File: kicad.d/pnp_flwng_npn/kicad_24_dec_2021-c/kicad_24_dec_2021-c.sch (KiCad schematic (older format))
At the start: 30 parts, among them Q1 2N3906, SW1 SW_SPDT, U1 ULN2803A

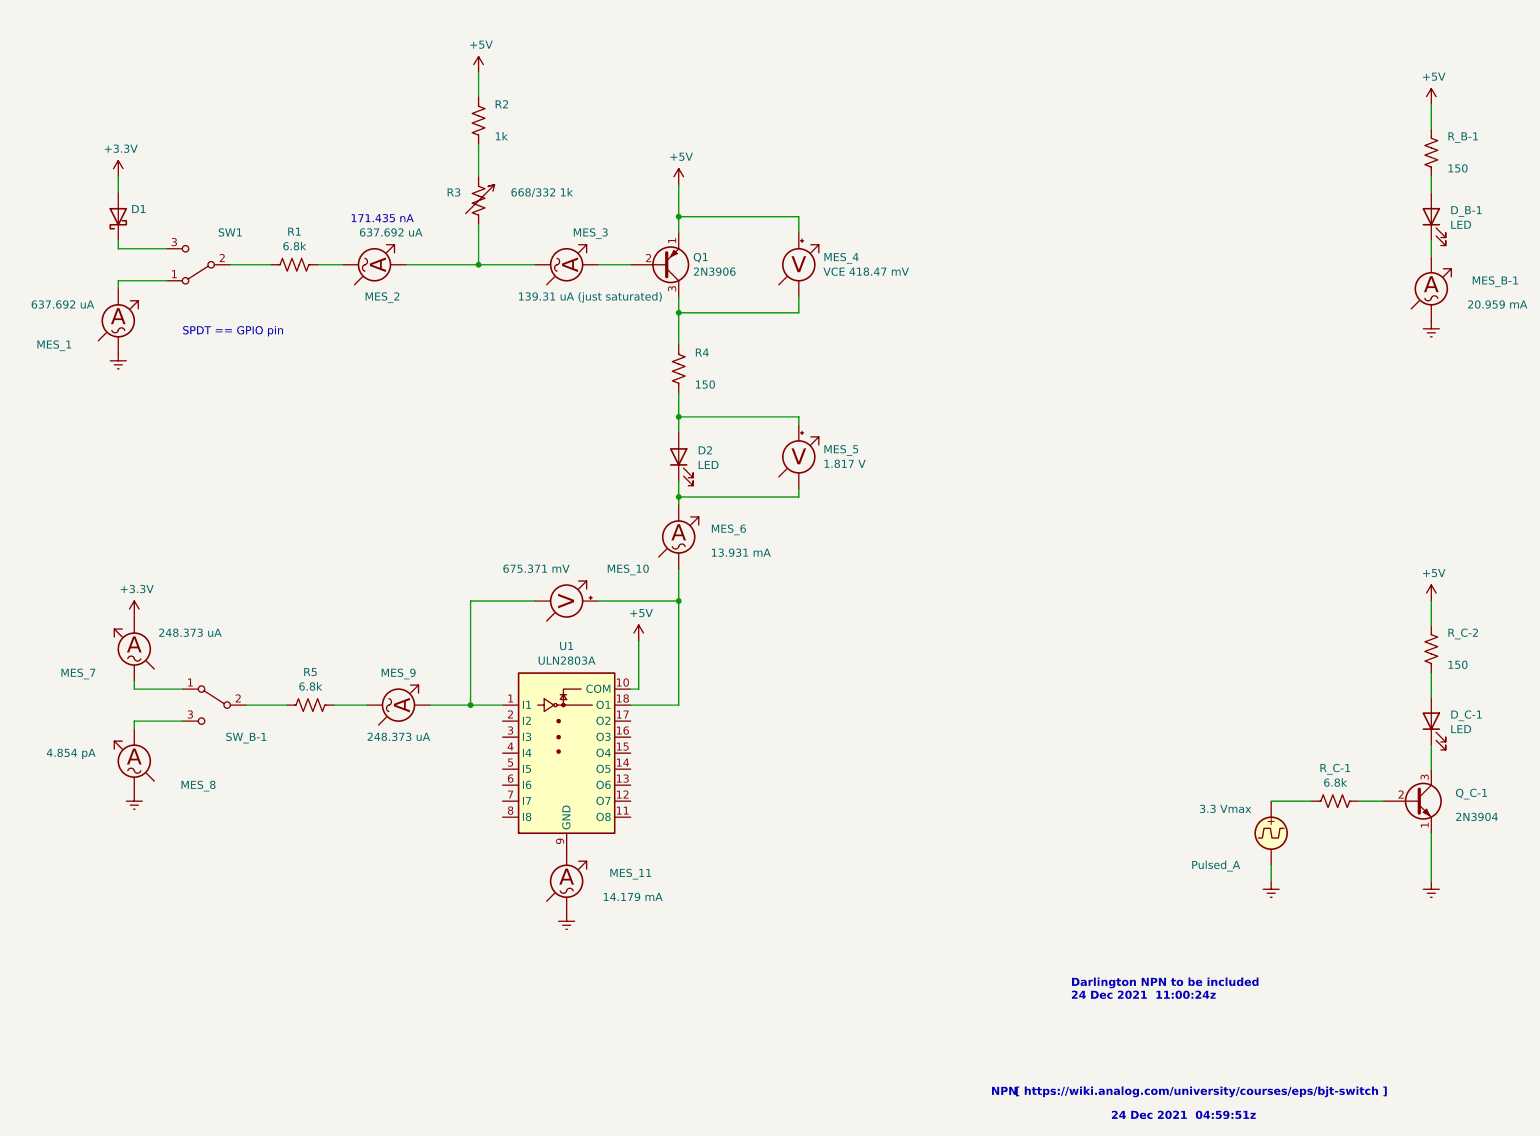
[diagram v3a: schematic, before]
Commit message: AC ammeter to DC
	modified:   kicad_24_dec_2021-c-cache.lib
	modified:   kicad_24_dec_2021-c.png
	modified:   kicad_24_dec_2021-c.sch
	modified:   kicad_24_dec_2021-c.svg

On branch dvlp-aa
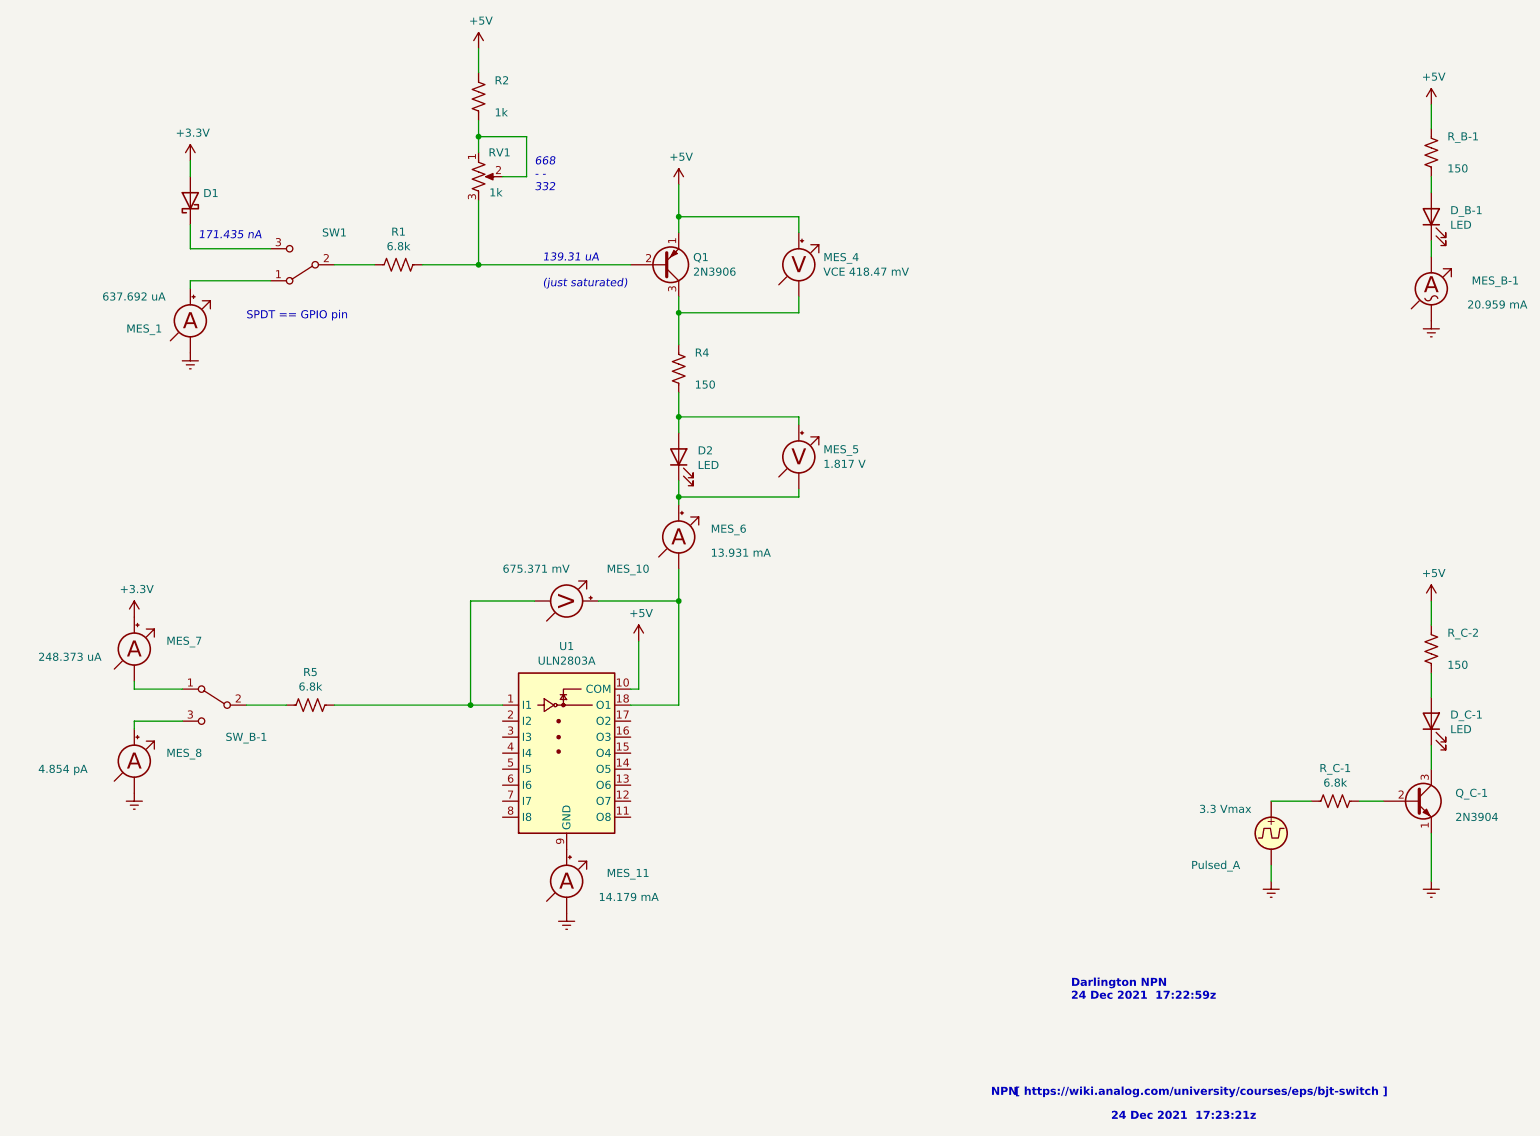
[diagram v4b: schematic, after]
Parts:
- removed MES_1, MES_2: 637.692 uA, symbol Device:Amperemeter_AC
- removed MES_11: 14.179 mA, symbol Device:Amperemeter_AC
- removed MES_3: 139.31 uA (just saturated), symbol Device:Amperemeter_AC
- removed MES_6: 13.931 mA, symbol Device:Amperemeter_AC
- removed MES_7, MES_9: 248.373 uA, symbol Device:Amperemeter_AC
- removed MES_8: 4.854 pA, symbol Device:Amperemeter_AC
- removed R3: 668/332 1k, symbol Device:R_Variable_US
- added MES_1: 637.692 uA, symbol Device:Amperemeter_DC
- added MES_11: 14.179 mA, symbol Device:Amperemeter_DC
- added MES_6: 13.931 mA, symbol Device:Amperemeter_DC
- added MES_7: 248.373 uA, symbol Device:Amperemeter_DC
- added MES_8: 4.854 pA, symbol Device:Amperemeter_DC
- added RV1: 1k, symbol Device:R_POT_US
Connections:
- net +3V3: now also MES_7.2 (+)
- net GNDREF: now also MES_1.1 (-), MES_11.1 (-), MES_8.1 (-)
- net at MES_10.1 (-), U1.1 (I1): now also R5.2
- net at MES_10.2 (+), U1.18 (O1): now also MES_6.1 (-)
- net at U1.9 (GND): now also MES_11.2 (+)
- net at D2.1 (K), MES_5.1 (-): now also MES_6.2 (+)
- net at SW_B-1.1 (A): now also MES_7.1 (-)
- net at SW_B-1.3 (C): now also MES_8.2 (+)
- net at Q1.2 (B): now also R1.2, RV1.3
- net at R2.2: now also RV1.1, RV1.2
- net at SW1.1 (A): now also MES_1.2 (+)
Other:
- note added: "139.31 uA\n\n(just saturated)"
- note added: "24 Dec 2021 17:23:21z"
- note added: "668\n- -\n332"
- note added: "Darlington NPN \n24 Dec 2021 17:22:59z"
- note removed: "24 Dec 2021 04:59:51z"
- note removed: "Darlington NPN to be included\n24 Dec 2021 11:00:24z"
- moved on the sheet: D1, R1, R2, SW1
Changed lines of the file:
@@
 $EndDescr
-$Comp
-L Device:Amperemeter_AC MES_6
-U 1 1 61D27D60
-P 5500 4000
-F 0 "MES_6" H 5700 4050 50  0000 L CNN
-F 1 "13.931 mA" H 5700 3900 50  0000 L CNN
-F 2 "" V 5500 4100 50  0001 C CNN
-F 3 "~" V 5500 4100 50  0001 C CNN
-	1    5500 4000
-	1    0    0    -1
-$EndComp
 $Comp
 L Device:LED D2
@@
  [ https://wiki.analog.com/university/courses/eps/bjt-switch ]
 Text Notes 8200 7650 0    50   ~ 10
-24 Dec 2021  04:59:51z
+24 Dec 2021  17:23:21z
 $Comp
 L Switch:SW_SPDT SW_B-1
@@
 $EndComp
 Wire Wire Line
-	3350 5050 3550 5050
-Wire Wire Line
 	2800 5050 3050 5050
 $Comp
@@
 $EndComp
 $Comp
-L Device:Amperemeter_AC MES_8
-U 1 1 61D1013E
-P 2100 5400
-F 0 "MES_8" H 1700 5250 50  0000 C CNN
-F 1 "4.854 pA" H 2650 5450 50  0000 R CNN
-F 2 "" V 2100 5500 50  0001 C CNN
-F 3 "~" V 2100 5500 50  0001 C CNN
-	1    2100 5400
-	-1   0    0    -1
-$EndComp
-$Comp
-L Device:Amperemeter_AC MES_7
-U 1 1 61D16E82
-P 2100 4700
-F 0 "MES_7" H 2450 4550 50  0000 C CNN
-F 1 "248.373 uA" H 1950 4800 50  0000 R CNN
-F 2 "" V 2100 4800 50  0001 C CNN
-F 3 "~" V 2100 4800 50  0001 C CNN
-	1    2100 4700
-	-1   0    0    -1
-$EndComp
-$Comp
 L power:+3.3V #PWR?
 U 1 1 61C80D01
@@
 	2100 5150 2100 5200
 $Comp
-L Device:Amperemeter_AC MES_9
-U 1 1 61C9332E
-P 3750 5050
-F 0 "MES_9" V 3950 5050 50  0000 C CNN
-F 1 "248.373 uA" V 3550 5050 50  0000 C CNN
-F 2 "" V 3750 5150 50  0001 C CNN
-F 3 "~" V 3750 5150 50  0001 C CNN
-	1    3750 5050
-	0    1    -1   0
-$EndComp
-Wire Wire Line
-	3950 5050 4200 5050
-$Comp
 L Device:LED D_B-1
 U 1 1 61E20E38
@@
 	5500 3750 5500 3800
 Text Notes 7950 6900 0    50   ~ 10
-Darlington NPN to be included\n24 Dec 2021  11:00:24z
+Darlington NPN \n24 Dec 2021  17:22:59z
 $Comp
 L Transistor_BJT:2N3904 Q_C-1
@@
 $EndComp
 $Comp
-L Device:Amperemeter_AC MES_11
-U 1 1 61C983D6
-P 4800 6150
-F 0 "MES_11" H 5200 6200 50  0000 C CNN
-F 1 "14.179 mA" H 5400 6050 50  0000 R CNN
-F 2 "" V 4800 6250 50  0001 C CNN
-F 3 "~" V 4800 6250 50  0001 C CNN
-	1    4800 6150
-	1    0    0    -1
-$EndComp
-$Comp
 L power:GNDREF #PWR?
 U 1 1 61C983DC
@@
 Wire Wire Line
 	5200 5050 5500 5050
-Connection ~ 4200 5050
 Wire Wire Line
 	5500 5050 5500 4400
@@
 Wire Wire Line
 	5500 2500 5500 2600
-$Comp
-L Device:Amperemeter_AC MES_3
-U 1 1 61D86C14
-P 4800 2300
-F 0 "MES_3" V 5000 2450 50  0000 C CNN
-F 1 "139.31 uA (just saturated)" V 4600 2900 50  0000 R CNN
-F 2 "" V 4800 2400 50  0001 C CNN
-F 3 "~" V 4800 2400 50  0001 C CNN
-	1    4800 2300
-	0    1    -1   0
-$EndComp
-Wire Wire Line
-	5000 2300 5200 2300
-Wire Wire Line
-	4600 2300 4250 2300
-Wire Wire Line
-	4250 2300 4250 2050
+Wire Wire Line
+	4250 2300 4250 1900
 $Comp
 L Device:R_US R2
 U 1 1 61DAD537
-P 4250 1400
-F 0 "R2" H 4350 1500 50  0000 L CNN
-F 1 "1k" H 4350 1300 50  0000 L CNN
-F 2 "" V 4290 1390 50  0001 C CNN
-F 3 "~" H 4250 1400 50  0001 C CNN
-	1    4250 1400
-	1    0    0    -1
-$EndComp
-$Comp
-L Device:R_Variable_US R3
-U 1 1 61DB1117
-P 4250 1900
-F 0 "R3" H 4050 1950 50  0000 L CNN
-F 1 "668/332 1k" H 4450 1950 50  0000 L CNN
-F 2 "" V 4180 1900 50  0001 C CNN
-F 3 "~" H 4250 1900 50  0001 C CNN
-	1    4250 1900
+P 4250 1250
+F 0 "R2" H 4350 1350 50  0000 L CNN
+F 1 "1k" H 4350 1150 50  0000 L CNN
+F 2 "" V 4290 1240 50  0001 C CNN
+F 3 "~" H 4250 1250 50  0001 C CNN
+	1    4250 1250
 	1    0    0    -1
 $EndComp
@@
 L Device:R_US R1
 U 1 1 61DBDEB0
-P 3100 2300
-F 0 "R1" V 3305 2300 50  0000 C CNN
-F 1 "6.8k" V 3214 2300 50  0000 C CNN
-F 2 "" V 3140 2290 50  0001 C CNN
-F 3 "~" H 3100 2300 50  0001 C CNN
-	1    3100 2300
-	0    -1   -1   0
-$EndComp
-Wire Wire Line
-	2700 2300 2950 2300
+P 3750 2300
+F 0 "R1" V 3955 2300 50  0000 C CNN
+F 1 "6.8k" V 3864 2300 50  0000 C CNN
+F 2 "" V 3790 2290 50  0001 C CNN
+F 3 "~" H 3750 2300 50  0001 C CNN
+	1    3750 2300
+	0    -1   -1   0
+$EndComp
+Wire Wire Line
+	3350 2300 3600 2300
 $Comp
 L power:GNDREF #PWR?
 U 1 1 61DBDEBD
-P 2000 2850
-F 0 "#PWR?" H 2000 2600 50  0001 C CNN
-F 1 "GNDREF" H 2005 2677 50  0001 C CNN
-F 2 "" H 2000 2850 50  0001 C CNN
-F 3 "" H 2000 2850 50  0001 C CNN
-	1    2000 2850
-	1    0    0    -1
-$EndComp
-$Comp
-L Device:Amperemeter_AC MES_1
-U 1 1 61DBDEC3
-P 2000 2650
-F 0 "MES_1" H 1600 2500 50  0000 C CNN
-F 1 "637.692 uA" H 1850 2750 50  0000 R CNN
-F 2 "" V 2000 2750 50  0001 C CNN
-F 3 "~" V 2000 2750 50  0001 C CNN
-	1    2000 2650
+P 2450 2850
+F 0 "#PWR?" H 2450 2600 50  0001 C CNN
+F 1 "GNDREF" H 2455 2677 50  0001 C CNN
+F 2 "" H 2450 2850 50  0001 C CNN
+F 3 "" H 2450 2850 50  0001 C CNN
+	1    2450 2850
 	1    0    0    -1
 $EndComp
@@
 L power:+3.3V #PWR?
 U 1 1 61DBDECF
-P 2000 1750
-F 0 "#PWR?" H 2000 1600 50  0001 C CNN
-F 1 "+3.3V" H 2015 1923 50  0000 C CNN
-F 2 "" H 2000 1750 50  0001 C CNN
-F 3 "" H 2000 1750 50  0001 C CNN
-	1    2000 1750
-	1    0    0    -1
-$EndComp
-Wire Wire Line
-	2300 2200 2000 2200
-Wire Wire Line
-	2000 2200 2000 2150
-Wire Wire Line
-	2300 2400 2000 2400
-Wire Wire Line
-	2000 2400 2000 2450
+P 2450 1650
+F 0 "#PWR?" H 2450 1500 50  0001 C CNN
+F 1 "+3.3V" H 2465 1823 50  0000 C CNN
+F 2 "" H 2450 1650 50  0001 C CNN
+F 3 "" H 2450 1650 50  0001 C CNN
+	1    2450 1650
+	1    0    0    -1
+$EndComp
+Wire Wire Line
+	2950 2200 2450 2200
+Wire Wire Line
+	2450 2200 2450 2050
+Wire Wire Line
+	2950 2400 2450 2400
+Wire Wire Line
+	2450 2400 2450 2450
 $Comp
 L Device:D_Schottky D1
 U 1 1 61DC0D35
-P 2000 2000
-F 0 "D1" V 2046 1920 50  0000 R CNN
-F 1 "Schottky" V 1950 2450 50  0001 R CNN
-F 2 "" H 2000 2000 50  0001 C CNN
-F 3 "~" H 2000 2000 50  0001 C CNN
-	1    2000 2000
-	0    -1   -1   0
-$EndComp
-Wire Wire Line
-	2000 1750 2000 1850
-$Comp
-L Device:Amperemeter_AC MES_2
-U 1 1 61DCD5C7
-P 3600 2300
-F 0 "MES_2" V 3400 2350 50  0000 C CNN
-F 1 "637.692 uA" V 3800 2600 50  0000 R CNN
-F 2 "" V 3600 2400 50  0001 C CNN
-F 3 "~" V 3600 2400 50  0001 C CNN
-	1    3600 2300
-	0    1    -1   0
-$EndComp
-Text Notes 2400 2750 0    50   ~ 0
+P 2450 1900
+F 0 "D1" V 2496 1820 50  0000 R CNN
+F 1 "Schottky" V 2400 2350 50  0001 R CNN
+F 2 "" H 2450 1900 50  0001 C CNN
+F 3 "~" H 2450 1900 50  0001 C CNN
+	1    2450 1900
+	0    -1   -1   0
+$EndComp
+Wire Wire Line
+	2450 1650 2450 1750
+Text Notes 2800 2650 0    50   ~ 0
 SPDT == GPIO pin
 Wire Wire Line
-	3250 2300 3400 2300
-Wire Wire Line
-	4250 1550 4250 1750
-Wire Wire Line
-	3800 2300 4250 2300
-Connection ~ 4250 2300
-Wire Wire Line
-	4250 1100 4250 1250
+	3900 2300 4250 2300
+Wire Wire Line
+	4250 1400 4250 1500
+Wire Wire Line
+	4250 950  4250 1100
 $Comp
 L power:+5V #PWR?
 U 1 1 61DF9556
-P 4250 1100
-F 0 "#PWR?" H 4250 950 50  0001 C CNN
-F 1 "+5V" H 4265 1273 50  0000 C CNN
-F 2 "" H 4250 1100 50  0001 C CNN
-F 3 "" H 4250 1100 50  0001 C CNN
-	1    4250 1100
+P 4250 950
+F 0 "#PWR?" H 4250 800 50  0001 C CNN
+F 1 "+5V" H 4265 1123 50  0000 C CNN
+F 2 "" H 4250 950 50  0001 C CNN
+F 3 "" H 4250 950 50  0001 C CNN
+	1    4250 950
 	1    0    0    -1
 $EndComp
@@
 L Switch:SW_SPDT SW1
 U 1 1 61DBDEB6
-P 2500 2300
-F 0 "SW1" H 2300 2100 50  0000 C CNN
-F 1 "SW_SPDT" H 2450 3300 50  0001 C CNN
-F 2 "" H 2500 2300 50  0001 C CNN
-F 3 "~" H 2500 2300 50  0001 C CNN
-	1    2500 2300
+P 3150 2300
+F 0 "SW1" H 2950 2100 50  0000 C CNN
+F 1 "SW_SPDT" H 3100 3300 50  0001 C CNN
+F 2 "" H 3150 2300 50  0001 C CNN
+F 3 "~" H 3150 2300 50  0001 C CNN
+	1    3150 2300
 	-1   0    0    1
 $EndComp
-Text Notes 3450 2050 0    50   ~ 0
+$Comp
+L Device:R_POT_US RV1
+U 1 1 61F13E8C
+P 4250 1750
+F 0 "RV1" H 4450 1900 50  0000 R CNN
+F 1 "1k" H 4400 1650 50  0000 R CNN
+F 2 "" H 4250 1750 50  0001 C CNN
+F 3 "~" H 4250 1750 50  0001 C CNN
+	1    4250 1750
+	1    0    0    -1
+$EndComp
+Wire Wire Line
+	4400 1750 4550 1750
+Wire Wire Line
+	4550 1500 4250 1500
+Connection ~ 4250 1500
+Wire Wire Line
+	4250 1500 4250 1600
+Wire Wire Line
+	4550 1750 4550 1500
+Text Notes 4600 1850 0    50   Italic 0
+668\n- -\n332
+$Comp
+L Device:Amperemeter_DC MES_7
+U 1 1 61F749E8
+P 2100 4700
+F 0 "MES_7" H 2300 4750 50  0000 L CNN
+F 1 "248.373 uA" H 1500 4650 50  0000 L CNN
+F 2 "" V 2100 4800 50  0001 C CNN
+F 3 "~" V 2100 4800 50  0001 C CNN
+	1    2100 4700
+	1    0    0    -1
+$EndComp
+$Comp
+L Device:Amperemeter_DC MES_8
+U 1 1 61F93748
+P 2100 5400
+F 0 "MES_8" H 2300 5450 50  0000 L CNN
+F 1 "4.854 pA" H 1500 5350 50  0000 L CNN
+F 2 "" V 2100 5500 50  0001 C CNN
+F 3 "~" V 2100 5500 50  0001 C CNN
+	1    2100 5400
+	1    0    0    -1
+$EndComp
+$Comp
+L Device:Amperemeter_DC MES_1
+U 1 1 61F9B635
+P 2450 2650
+F 0 "MES_1" H 2050 2600 50  0000 L CNN
+F 1 "637.692 uA" H 1900 2800 50  0000 L CNN
+F 2 "" V 2450 2750 50  0001 C CNN
+F 3 "~" V 2450 2750 50  0001 C CNN
+	1    2450 2650
+	1    0    0    -1
+$EndComp
+Text Notes 2500 2150 0    50   Italic 0
 171.435 nA
+Wire Wire Line
+	4250 2300 5200 2300
+Connection ~ 4250 2300
+Text Notes 4650 2450 0    50   Italic 0
+  139.31 uA\n\n(just saturated)
+Wire Wire Line
+	3350 5050 4200 5050
+Connection ~ 4200 5050
+$Comp
+L Device:Amperemeter_DC MES_6
+U 1 1 62053A23
+P 5500 4000
+F 0 "MES_6" H 5700 4050 50  0000 L CNN
+F 1 "13.931 mA" H 5700 3900 50  0000 L CNN
+F 2 "" V 5500 4100 50  0001 C CNN
+F 3 "~" V 5500 4100 50  0001 C CNN
+	1    5500 4000
+	1    0    0    -1
+$EndComp
+$Comp
+L Device:Amperemeter_DC MES_11
+U 1 1 62071491
+P 4800 6150
+F 0 "MES_11" H 5050 6200 50  0000 L CNN
+F 1 "14.179 mA" H 5000 6050 50  0000 L CNN
+F 2 "" V 4800 6250 50  0001 C CNN
+F 3 "~" V 4800 6250 50  0001 C CNN
+	1    4800 6150
+	1    0    0    -1
+$EndComp
 $EndSCHEMATC

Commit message: Further modifications for correctness
	modified:   kicad_24_dec_2021-c.png
	modified:   kicad_24_dec_2021-c.sch
	modified:   kicad_24_dec_2021-c.svg

On branch dvlp-aa
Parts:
- MES_8: value 4.854 pA -> -4.854 pA
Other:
- note added: "24 Dec 2021 17:40:45z"
- note added: "Darlington NPN \n24 Dec 2021 17:40:45z"
- note removed: "24 Dec 2021 17:23:21z"
- note removed: "Darlington NPN \n24 Dec 2021 17:22:59z"
- moved on the sheet: D1, D2, MES_1, MES_10, MES_11, MES_4, MES_5, MES_6, MES_7, MES_8, Q1, R1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
